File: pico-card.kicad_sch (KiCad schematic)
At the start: 0 parts

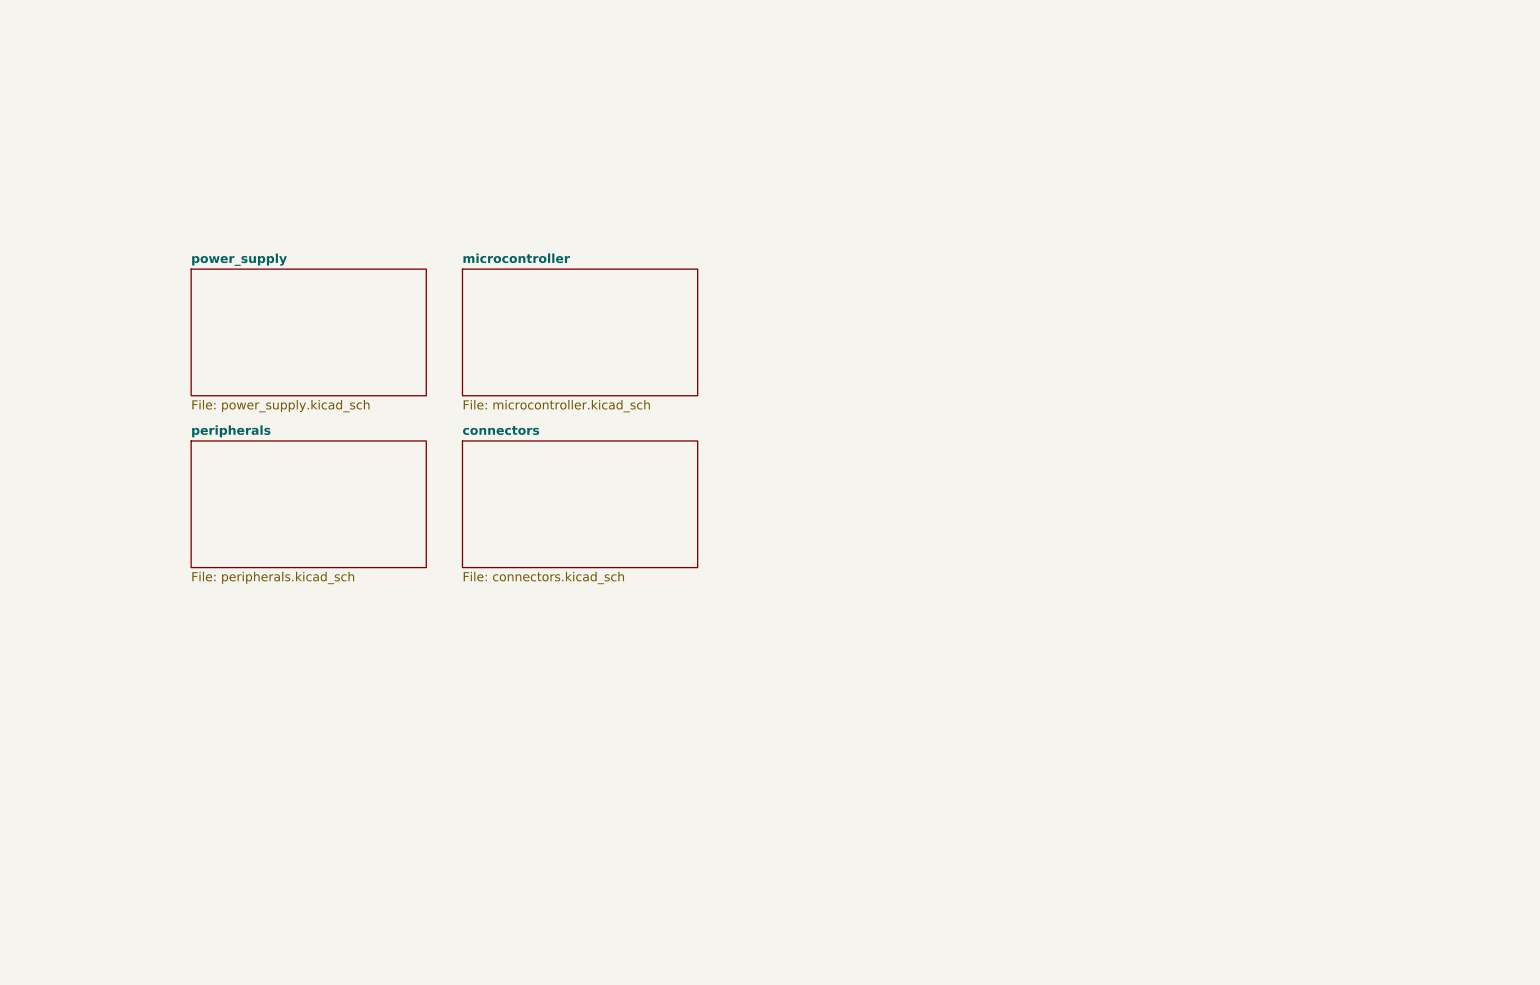
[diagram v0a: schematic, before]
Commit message: All component except led matrix
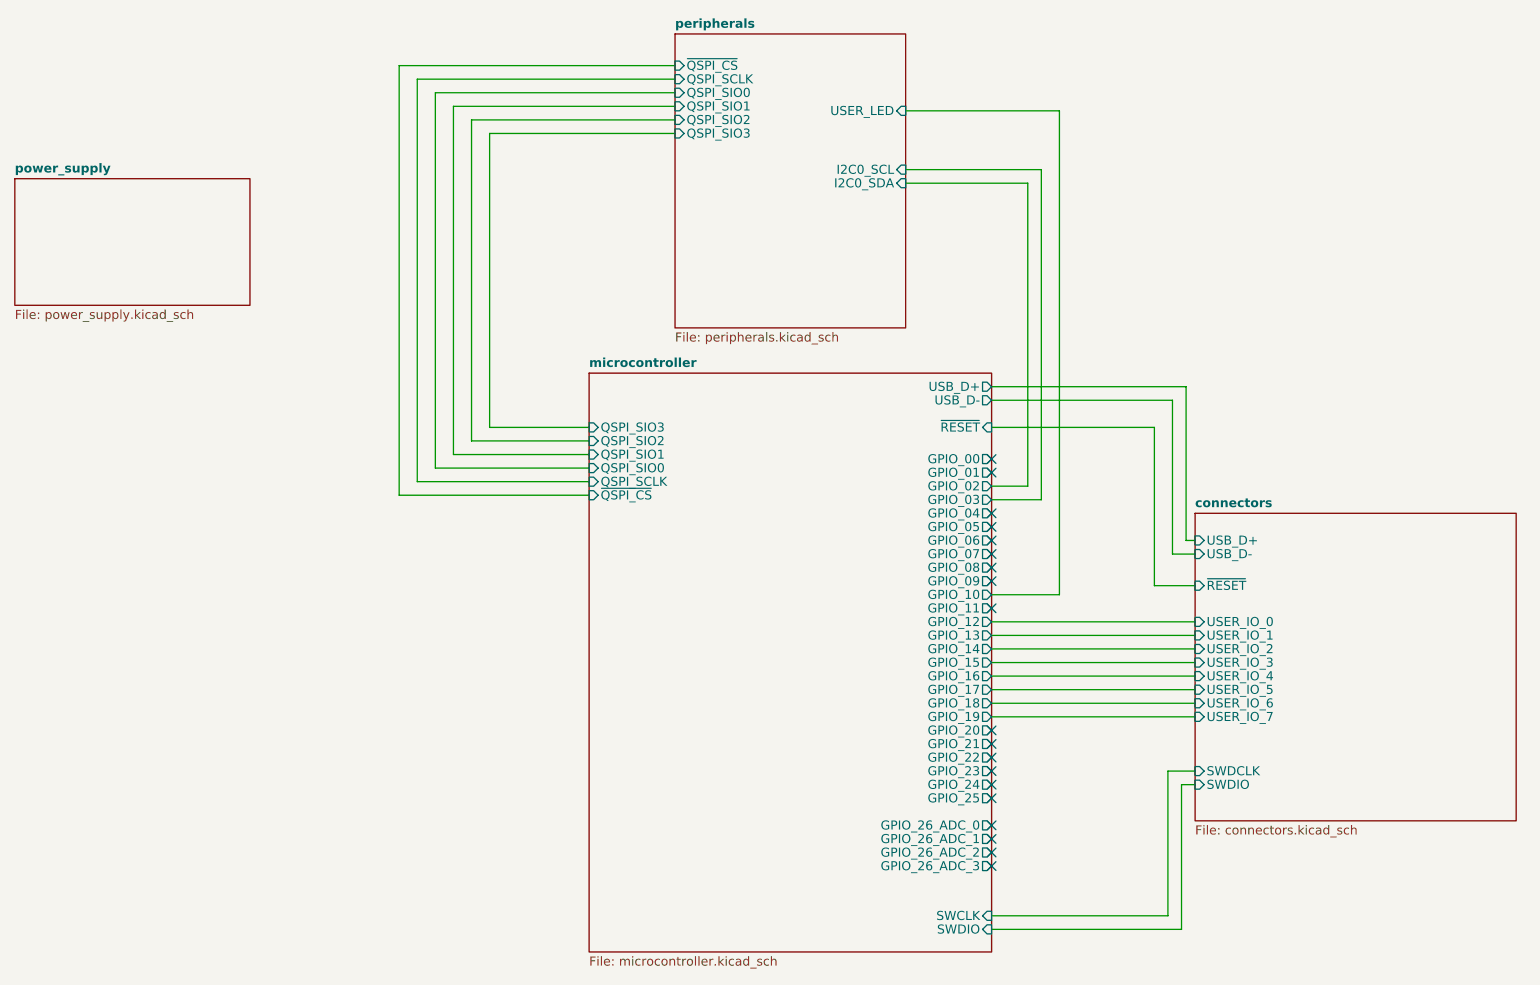
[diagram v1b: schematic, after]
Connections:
- no-connect marks 0 -> 19
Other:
- sheet connectors ports: added SWDCLK, SWDIO, USB_D+, USB_D-, USER_IO_0, USER_IO_1, USER_IO_2, USER_IO_3, USER_IO_4, USER_IO_5, USER_IO_6, USER_IO_7, ~{RESET}; removed none
- sheet microcontroller ports: added GPIO_00, GPIO_01, GPIO_02, GPIO_03, GPIO_04, GPIO_05, GPIO_06, GPIO_07, GPIO_08, GPIO_09, GPIO_10, GPIO_11, GPIO_12, GPIO_13, GPIO_14, GPIO_15, GPIO_16, GPIO_17, GPIO_18, GPIO_19, GPIO_20, GPIO_21, GPIO_22, GPIO_23, GPIO_24, GPIO_25, GPIO_26_ADC_0, GPIO_26_ADC_1, GPIO_26_ADC_2, GPIO_26_ADC_3, QSPI_SCLK, QSPI_SIO0, QSPI_SIO1, QSPI_SIO2, QSPI_SIO3, SWCLK, SWDIO, USB_D+, USB_D-, ~{QSPI_CS}, ~{RESET}; removed none
- sheet peripherals ports: added I2C0_SCL, I2C0_SDA, QSPI_SCLK, QSPI_SIO0, QSPI_SIO1, QSPI_SIO2, QSPI_SIO3, USER_LED, ~{QSPI_CS}; removed none

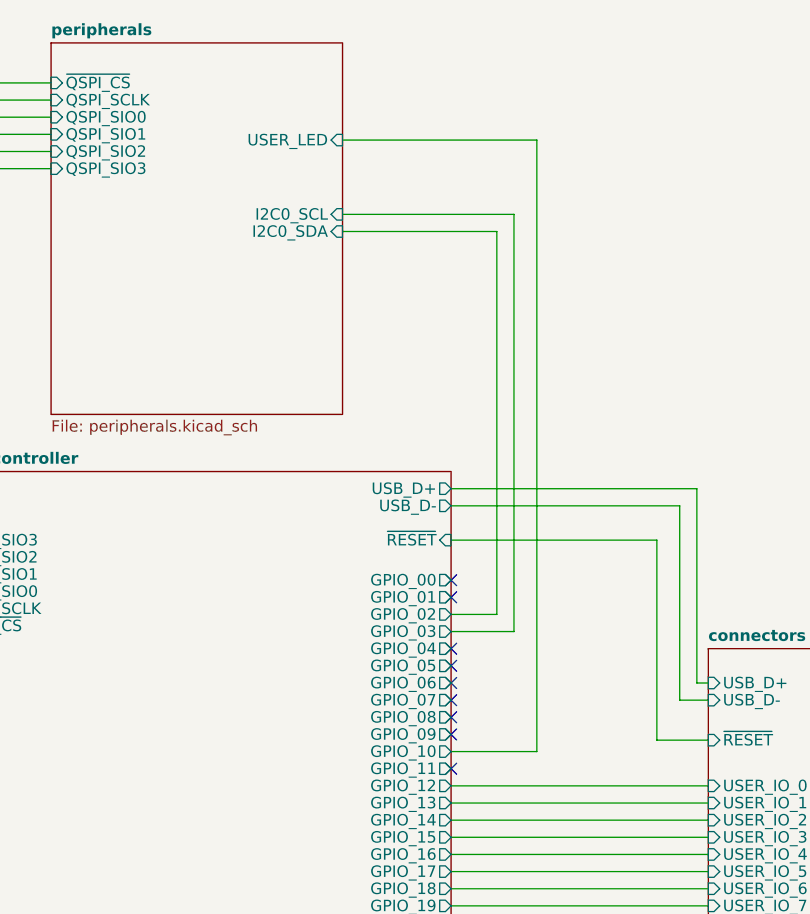
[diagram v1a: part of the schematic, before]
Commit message: finish schematic, prep pcb
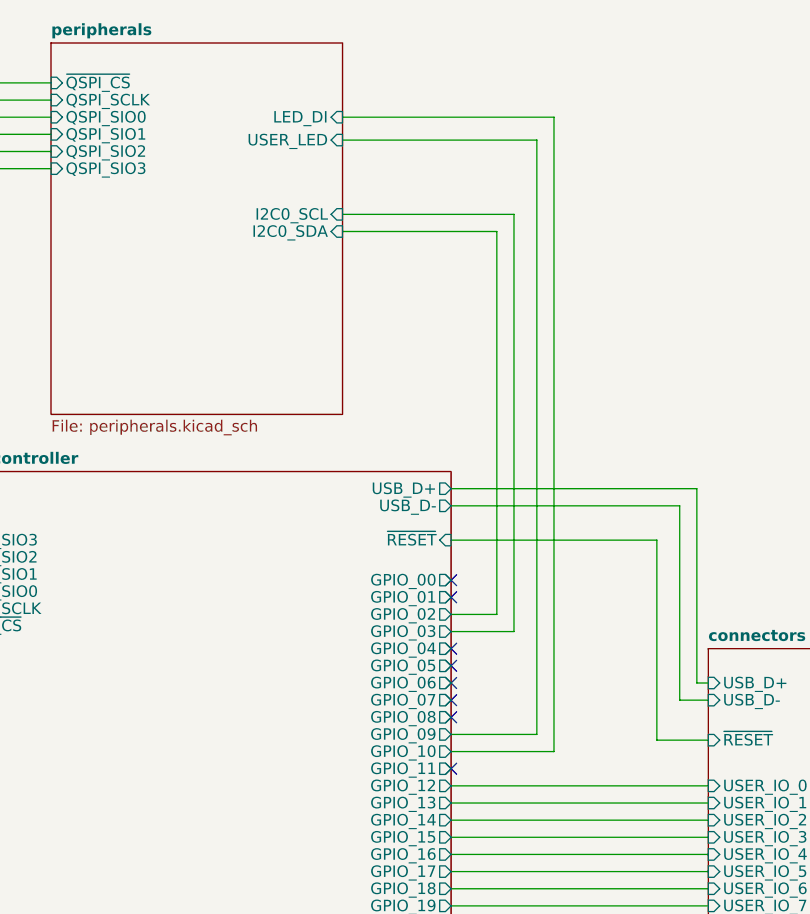
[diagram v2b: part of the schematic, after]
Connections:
- no-connect marks 19 -> 18
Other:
- sheet peripherals ports: added LED_DI; removed none

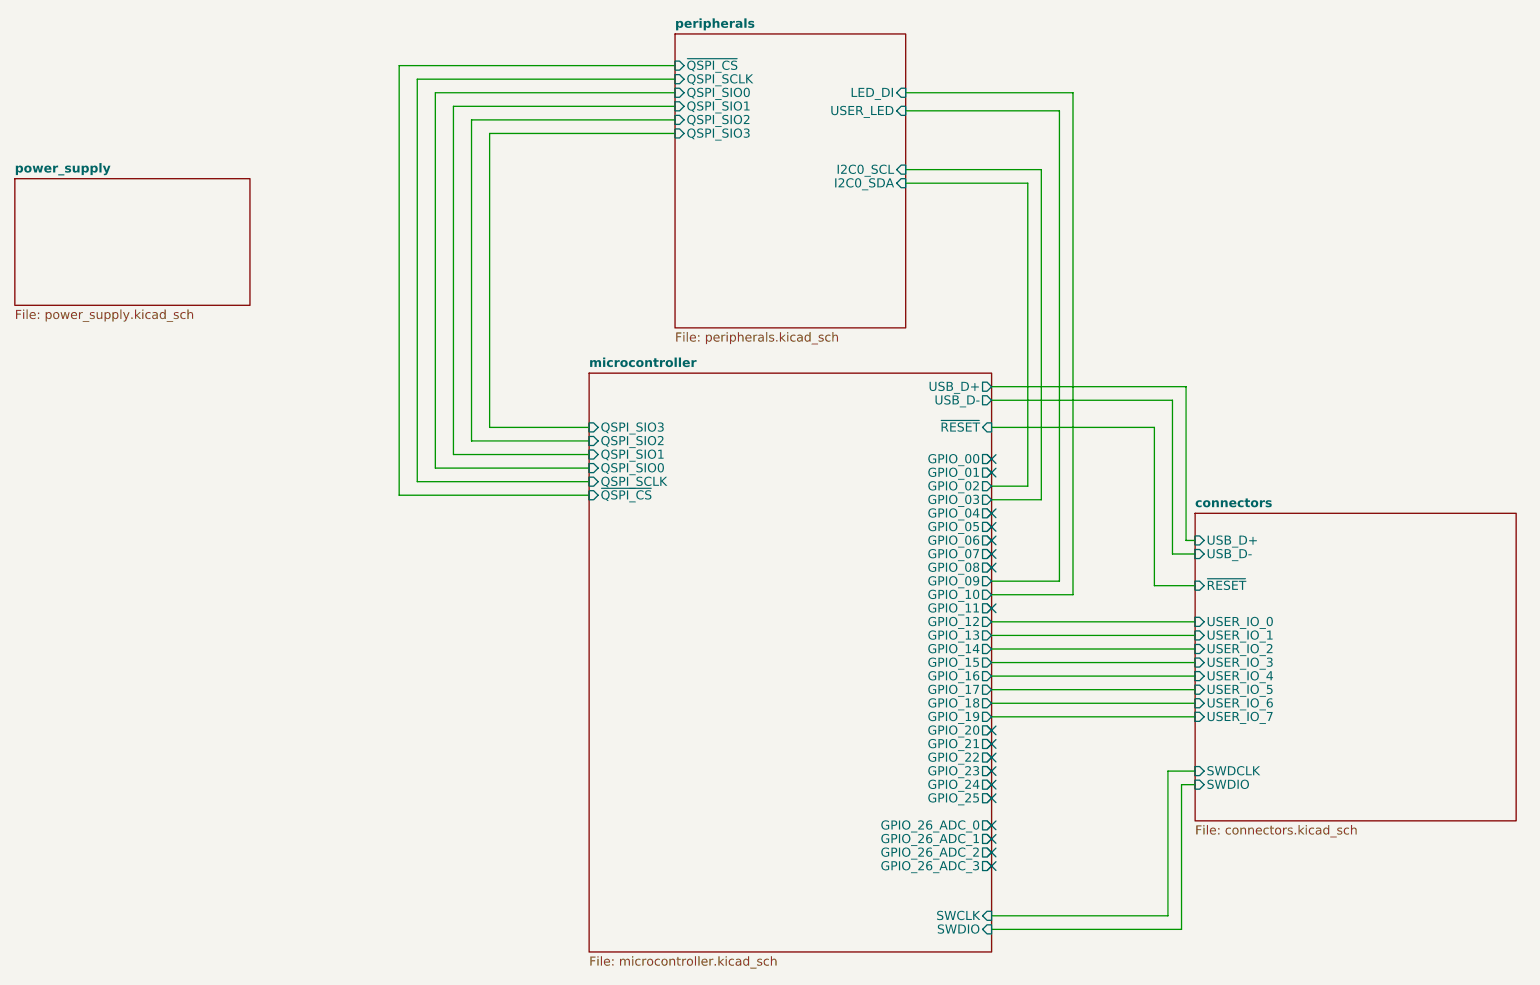
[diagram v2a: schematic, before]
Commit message: Basic routing MCU, crystal, flash, crypto
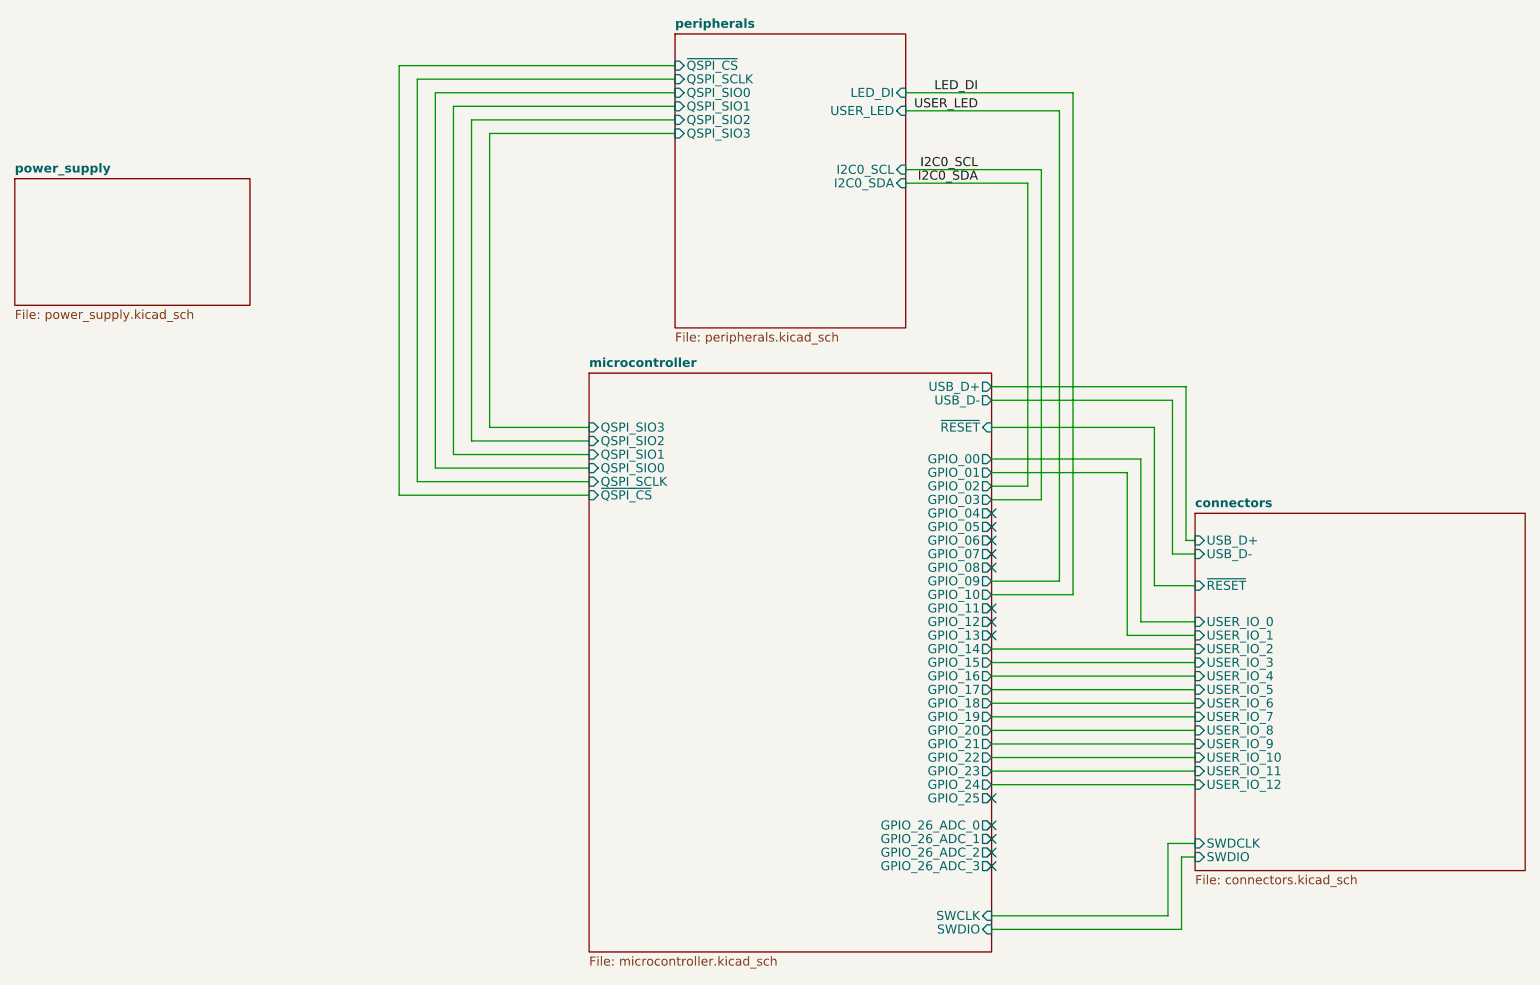
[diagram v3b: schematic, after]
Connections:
- no-connect marks 18 -> 13
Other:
- sheet connectors ports: added USER_IO_10, USER_IO_11, USER_IO_12, USER_IO_8, USER_IO_9; removed none
